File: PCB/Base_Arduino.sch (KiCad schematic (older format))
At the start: 16 parts, among them IC1 ATMEGA328-P, X1 CRYSTAL

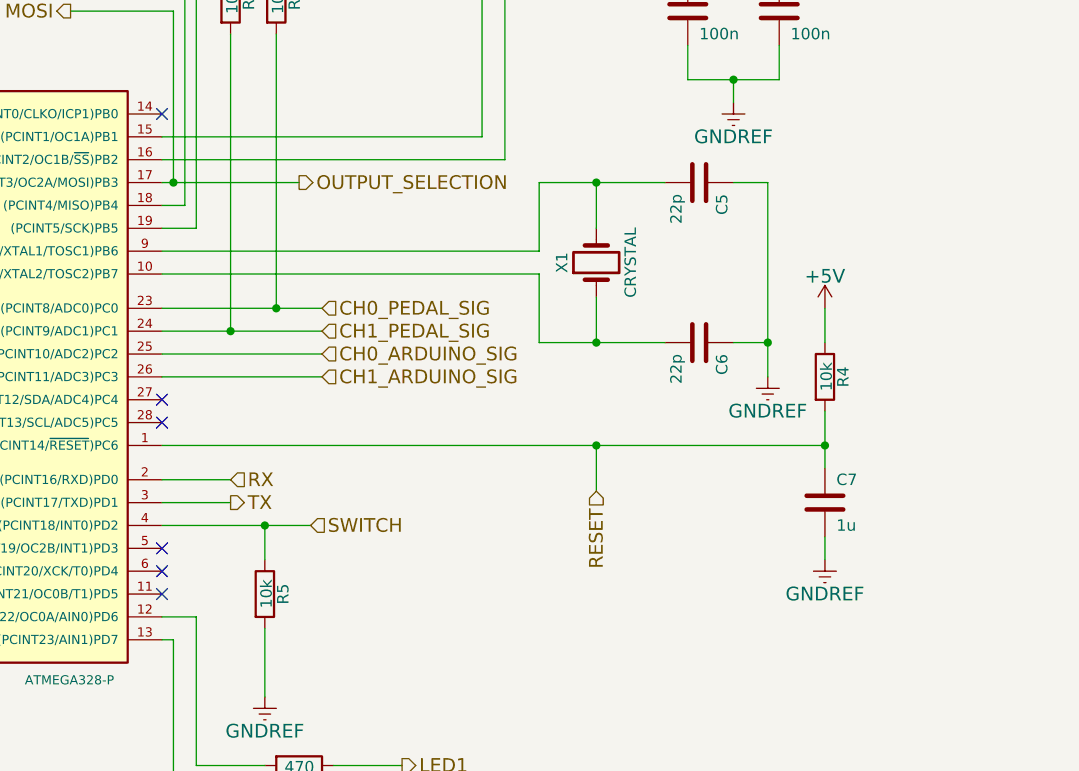
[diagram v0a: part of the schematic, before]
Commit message: Optional crystal resistor.
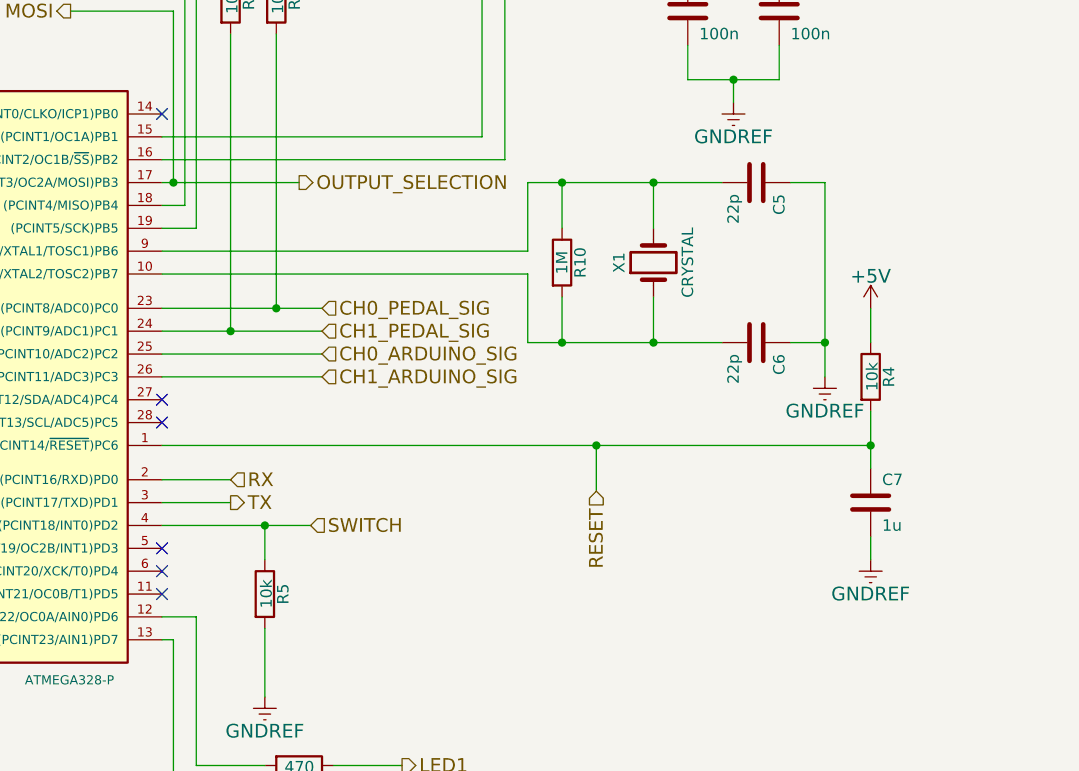
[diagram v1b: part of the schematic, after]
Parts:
- added R10: 1M, symbol R
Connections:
- net at C6.2, IC1.10 ((PCINT7/XTAL2/TOSC2)PB7), X1.1: now also R10.2
- net at C5.2, IC1.9 ((PCINT6/XTAL1/TOSC1)PB6), X1.2: now also R10.1
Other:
- moved on the sheet: C5, C6, C7, R4, X1
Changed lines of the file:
@@
 $EndComp
 $Comp
-L GNDREF #PWR015
+L GNDREF #PWR15
 U 1 1 54D7F6B2
 P 2550 5150
-F 0 "#PWR015" H 2550 4900 60  0001 C CNN
+F 0 "#PWR15" H 2550 4900 60  0001 C CNN
 F 1 "GNDREF" H 2550 5000 60  0000 C CNN
 F 2 "" H 2550 5150 60  0000 C CNN
@@
 NoConn ~ 2700 3250
 $Comp
-L +5V #PWR016
+L +5V #PWR14
 U 1 1 54D7F7B3
 P 2550 2300
-F 0 "#PWR016" H 2550 2150 60  0001 C CNN
+F 0 "#PWR14" H 2550 2150 60  0001 C CNN
 F 1 "+5V" H 2550 2440 60  0000 C CNN
 F 2 "" H 2550 2300 60  0000 C CNN
@@
 L Crystal X1
 U 1 1 54D7F8BC
-P 6500 3300
-F 0 "X1" H 6500 3450 50  0000 C CNN
-F 1 "CRYSTAL" H 6500 3150 50  0000 C CNN
-F 2 "Crystals:Crystal_HC50-U_Vertical" H 6500 3300 60  0001 C CNN
-F 3 "" H 6500 3300 60  0000 C CNN
-	1    6500 3300
+P 6750 3300
+F 0 "X1" H 6750 3450 50  0000 C CNN
+F 1 "CRYSTAL" H 6750 3150 50  0000 C CNN
+F 2 "Crystals:Crystal_HC50-U_Vertical" H 6750 3300 60  0001 C CNN
+F 3 "" H 6750 3300 60  0000 C CNN
+	1    6750 3300
 	0    -1   -1   0
 $EndComp
@@
 L C C5
 U 1 1 54D7FA47
-P 6950 2950
-F 0 "C5" H 7000 3050 50  0000 L CNN
-F 1 "22p" H 7000 2850 50  0000 L CNN
-F 2 "Capacitors_ThroughHole:C_Rect_L7_W2_P5" H 6988 2800 30  0001 C CNN
-F 3 "" H 6950 2950 60  0000 C CNN
-	1    6950 2950
+P 7200 2950
+F 0 "C5" H 7250 3050 50  0000 L CNN
+F 1 "22p" H 7250 2850 50  0000 L CNN
+F 2 "Capacitors_ThroughHole:C_Rect_L7_W2_P5" H 7238 2800 30  0001 C CNN
+F 3 "" H 7200 2950 60  0000 C CNN
+	1    7200 2950
 	0    1    1    0
 $EndComp
@@
 L C C6
 U 1 1 54D7FAD7
-P 6950 3650
-F 0 "C6" H 7000 3750 50  0000 L CNN
-F 1 "22p" H 7000 3550 50  0000 L CNN
-F 2 "Capacitors_ThroughHole:C_Rect_L7_W2_P5" H 6988 3500 30  0001 C CNN
-F 3 "" H 6950 3650 60  0000 C CNN
-	1    6950 3650
-	0    1    1    0
-$EndComp
-$Comp
-L GNDREF #PWR017
+P 7200 3650
+F 0 "C6" H 7250 3750 50  0000 L CNN
+F 1 "22p" H 7250 3550 50  0000 L CNN
+F 2 "Capacitors_ThroughHole:C_Rect_L7_W2_P5" H 7238 3500 30  0001 C CNN
+F 3 "" H 7200 3650 60  0000 C CNN
+	1    7200 3650
+	0    1    1    0
+$EndComp
+$Comp
+L GNDREF #PWR19
 U 1 1 54D7FB6B
-P 7250 3800
-F 0 "#PWR017" H 7250 3550 60  0001 C CNN
-F 1 "GNDREF" H 7250 3650 60  0000 C CNN
-F 2 "" H 7250 3800 60  0000 C CNN
-F 3 "" H 7250 3800 60  0000 C CNN
-	1    7250 3800
-	1    0    0    -1
-$EndComp
-$Comp
-L GNDREF #PWR018
+P 7500 3800
+F 0 "#PWR19" H 7500 3550 60  0001 C CNN
+F 1 "GNDREF" H 7500 3650 60  0000 C CNN
+F 2 "" H 7500 3800 60  0000 C CNN
+F 3 "" H 7500 3800 60  0000 C CNN
+	1    7500 3800
+	1    0    0    -1
+$EndComp
+$Comp
+L GNDREF #PWR21
 U 1 1 54D7FCBC
-P 7500 4600
-F 0 "#PWR018" H 7500 4350 60  0001 C CNN
-F 1 "GNDREF" H 7500 4450 60  0000 C CNN
-F 2 "" H 7500 4600 60  0000 C CNN
-F 3 "" H 7500 4600 60  0000 C CNN
-	1    7500 4600
-	1    0    0    -1
-$EndComp
-$Comp
-L +5V #PWR019
+P 7700 4600
+F 0 "#PWR21" H 7700 4350 60  0001 C CNN
+F 1 "GNDREF" H 7700 4450 60  0000 C CNN
+F 2 "" H 7700 4600 60  0000 C CNN
+F 3 "" H 7700 4600 60  0000 C CNN
+	1    7700 4600
+	1    0    0    -1
+$EndComp
+$Comp
+L +5V #PWR20
 U 1 1 54D7FCD0
-P 7500 3500
-F 0 "#PWR019" H 7500 3350 60  0001 C CNN
-F 1 "+5V" H 7500 3640 60  0000 C CNN
-F 2 "" H 7500 3500 60  0000 C CNN
-F 3 "" H 7500 3500 60  0000 C CNN
-	1    7500 3500
+P 7700 3500
+F 0 "#PWR20" H 7700 3350 60  0001 C CNN
+F 1 "+5V" H 7700 3640 60  0000 C CNN
+F 2 "" H 7700 3500 60  0000 C CNN
+F 3 "" H 7700 3500 60  0000 C CNN
+	1    7700 3500
 	1    0    0    -1
 $EndComp
@@
 L C C7
 U 1 1 54D7FCE4
-P 7500 4350
-F 0 "C7" H 7550 4450 50  0000 L CNN
-F 1 "1u" H 7550 4250 50  0000 L CNN
-F 2 "Capacitors_ThroughHole:C_Rect_L7_W4.5_P5" H 7538 4200 30  0001 C CNN
-F 3 "" H 7500 4350 60  0000 C CNN
-	1    7500 4350
+P 7700 4350
+F 0 "C7" H 7750 4450 50  0000 L CNN
+F 1 "1u" H 7750 4250 50  0000 L CNN
+F 2 "Capacitors_ThroughHole:C_Rect_L7_W4.5_P5" H 7738 4200 30  0001 C CNN
+F 3 "" H 7700 4350 60  0000 C CNN
+	1    7700 4350
 	1    0    0    -1
 $EndComp
@@
 L R R4
 U 1 1 54D7FD1C
-P 7500 3800
-F 0 "R4" V 7580 3800 50  0000 C CNN
-F 1 "10k" V 7507 3801 50  0000 C CNN
-F 2 "Discret:R3" V 7430 3800 30  0001 C CNN
-F 3 "" H 7500 3800 30  0000 C CNN
-	1    7500 3800
+P 7700 3800
+F 0 "R4" V 7780 3800 50  0000 C CNN
+F 1 "10k" V 7707 3801 50  0000 C CNN
+F 2 "Discret:R3" V 7630 3800 30  0001 C CNN
+F 3 "" H 7700 3800 30  0000 C CNN
+	1    7700 3800
 	1    0    0    -1
 $EndComp
@@
 $EndComp
 $Comp
-L GNDREF #PWR020
+L GNDREF #PWR17
 U 1 1 54D8038E
 P 5050 5200
-F 0 "#PWR020" H 5050 4950 60  0001 C CNN
+F 0 "#PWR17" H 5050 4950 60  0001 C CNN
 F 1 "GNDREF" H 5050 5050 60  0000 C CNN
 F 2 "" H 5050 5200 60  0000 C CNN
@@
 $EndComp
 $Comp
-L +5V #PWR021
+L +5V #PWR16
 U 1 1 54D80C81
 P 5000 1700
-F 0 "#PWR021" H 5000 1550 60  0001 C CNN
+F 0 "#PWR16" H 5000 1550 60  0001 C CNN
 F 1 "+5V" H 5000 1840 60  0000 C CNN
 F 2 "" H 5000 1700 60  0000 C CNN
@@
 $EndComp
 $Comp
-L GNDREF #PWR022
+L GNDREF #PWR18
 U 1 1 54D8194E
 P 7100 2600
-F 0 "#PWR022" H 7100 2350 60  0001 C CNN
+F 0 "#PWR18" H 7100 2350 60  0001 C CNN
 F 1 "GNDREF" H 7100 2450 60  0000 C CNN
 F 2 "" H 7100 2600 60  0000 C CNN
@@
 CH0_ARDUINO_SIG
 $Comp
-L +5V #PWR023
+L +5V #PWR12
 U 1 1 57BC9586
 P 1650 3400
-F 0 "#PWR023" H 1650 3250 60  0001 C CNN
+F 0 "#PWR12" H 1650 3250 60  0001 C CNN
 F 1 "+5V" H 1650 3540 60  0000 C CNN
 F 2 "" H 1650 3400 60  0000 C CNN
@@
 $EndComp
 $Comp
-L GNDREF #PWR024
+L GNDREF #PWR13
 U 1 1 57BC95BE
 P 1650 3800
-F 0 "#PWR024" H 1650 3550 60  0001 C CNN
+F 0 "#PWR13" H 1650 3550 60  0001 C CNN
 F 1 "GNDREF" H 1650 3650 60  0000 C CNN
 F 2 "" H 1650 3800 60  0000 C CNN
@@
 Connection ~ 2550 2650
 Wire Wire Line
-	4600 3350 6250 3350
-Wire Wire Line
-	6250 3350 6250 3650
-Wire Wire Line
-	6250 3650 6800 3650
-Wire Wire Line
-	6500 3450 6500 3650
-Wire Wire Line
-	4600 3250 6250 3250
-Wire Wire Line
-	6250 3250 6250 2950
-Wire Wire Line
-	6250 2950 6800 2950
-Wire Wire Line
-	6500 2950 6500 3150
-Connection ~ 6500 3650
-Connection ~ 6500 2950
-Wire Wire Line
-	7250 2950 7250 3800
-Wire Wire Line
-	7100 2950 7250 2950
-Wire Wire Line
-	7100 3650 7250 3650
-Connection ~ 7250 3650
-Wire Wire Line
-	7500 4500 7500 4600
-Wire Wire Line
-	7500 3950 7500 4200
-Wire Wire Line
-	7500 3500 7500 3650
-Wire Wire Line
-	4600 4100 7500 4100
-Connection ~ 7500 4100
+	6200 3650 7050 3650
+Wire Wire Line
+	6750 3450 6750 3650
+Wire Wire Line
+	6200 2950 7050 2950
+Wire Wire Line
+	6750 2950 6750 3150
+Connection ~ 6750 3650
+Connection ~ 6750 2950
+Wire Wire Line
+	7500 2950 7500 3800
+Wire Wire Line
+	7350 2950 7500 2950
+Wire Wire Line
+	7350 3650 7500 3650
+Connection ~ 7500 3650
+Wire Wire Line
+	7700 4500 7700 4600
+Wire Wire Line
+	7700 3950 7700 4200
+Wire Wire Line
+	7700 3500 7700 3650
+Wire Wire Line
+	4600 4100 7700 4100
+Connection ~ 7700 4100
 Wire Wire Line
 	4600 4950 4650 4950
@@
 Wire Wire Line
 	4600 3800 5300 3800
+Wire Wire Line
+	6200 2950 6200 3250
+Wire Wire Line
+	6200 3650 6200 3350
+Wire Wire Line
+	6200 3350 4600 3350
+Wire Wire Line
+	6200 3250 4600 3250
+$Comp
+L R R10
+U 1 1 57BF3972
+P 6350 3300
+F 0 "R10" V 6430 3300 50  0000 C CNN
+F 1 "1M" V 6350 3300 50  0000 C CNN
+F 2 "" V 6280 3300 50  0000 C CNN
+F 3 "" H 6350 3300 50  0000 C CNN
+	1    6350 3300
+	1    0    0    -1
+$EndComp
+Wire Wire Line
+	6350 3150 6350 2950
+Connection ~ 6350 2950
+Wire Wire Line
+	6350 3450 6350 3650
+Connection ~ 6350 3650
 $EndSCHEMATC

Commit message: Resistor footprint.
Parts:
- R10: footprint (none) -> Discret:R3
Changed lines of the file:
@@
 $EndComp
 $Comp
-L GNDREF #PWR15
+L GNDREF #PWR015
 U 1 1 54D7F6B2
 P 2550 5150
-F 0 "#PWR15" H 2550 4900 60  0001 C CNN
+F 0 "#PWR015" H 2550 4900 60  0001 C CNN
 F 1 "GNDREF" H 2550 5000 60  0000 C CNN
 F 2 "" H 2550 5150 60  0000 C CNN
@@
 NoConn ~ 2700 3250
 $Comp
-L +5V #PWR14
+L +5V #PWR016
 U 1 1 54D7F7B3
 P 2550 2300
-F 0 "#PWR14" H 2550 2150 60  0001 C CNN
+F 0 "#PWR016" H 2550 2150 60  0001 C CNN
 F 1 "+5V" H 2550 2440 60  0000 C CNN
 F 2 "" H 2550 2300 60  0000 C CNN
@@
 $EndComp
 $Comp
-L GNDREF #PWR19
+L GNDREF #PWR017
 U 1 1 54D7FB6B
 P 7500 3800
-F 0 "#PWR19" H 7500 3550 60  0001 C CNN
+F 0 "#PWR017" H 7500 3550 60  0001 C CNN
 F 1 "GNDREF" H 7500 3650 60  0000 C CNN
 F 2 "" H 7500 3800 60  0000 C CNN
@@
 $EndComp
 $Comp
-L GNDREF #PWR21
+L GNDREF #PWR018
 U 1 1 54D7FCBC
 P 7700 4600
-F 0 "#PWR21" H 7700 4350 60  0001 C CNN
+F 0 "#PWR018" H 7700 4350 60  0001 C CNN
 F 1 "GNDREF" H 7700 4450 60  0000 C CNN
 F 2 "" H 7700 4600 60  0000 C CNN
@@
 $EndComp
 $Comp
-L +5V #PWR20
+L +5V #PWR019
 U 1 1 54D7FCD0
 P 7700 3500
-F 0 "#PWR20" H 7700 3350 60  0001 C CNN
+F 0 "#PWR019" H 7700 3350 60  0001 C CNN
 F 1 "+5V" H 7700 3640 60  0000 C CNN
 F 2 "" H 7700 3500 60  0000 C CNN
@@
 $EndComp
 $Comp
-L GNDREF #PWR17
+L GNDREF #PWR020
 U 1 1 54D8038E
 P 5050 5200
-F 0 "#PWR17" H 5050 4950 60  0001 C CNN
+F 0 "#PWR020" H 5050 4950 60  0001 C CNN
 F 1 "GNDREF" H 5050 5050 60  0000 C CNN
 F 2 "" H 5050 5200 60  0000 C CNN
@@
 $EndComp
 $Comp
-L +5V #PWR16
+L +5V #PWR021
 U 1 1 54D80C81
 P 5000 1700
-F 0 "#PWR16" H 5000 1550 60  0001 C CNN
+F 0 "#PWR021" H 5000 1550 60  0001 C CNN
 F 1 "+5V" H 5000 1840 60  0000 C CNN
 F 2 "" H 5000 1700 60  0000 C CNN
@@
 $EndComp
 $Comp
-L GNDREF #PWR18
+L GNDREF #PWR022
 U 1 1 54D8194E
 P 7100 2600
-F 0 "#PWR18" H 7100 2350 60  0001 C CNN
+F 0 "#PWR022" H 7100 2350 60  0001 C CNN
 F 1 "GNDREF" H 7100 2450 60  0000 C CNN
 F 2 "" H 7100 2600 60  0000 C CNN
@@
 CH0_ARDUINO_SIG
 $Comp
-L +5V #PWR12
+L +5V #PWR023
 U 1 1 57BC9586
 P 1650 3400
-F 0 "#PWR12" H 1650 3250 60  0001 C CNN
+F 0 "#PWR023" H 1650 3250 60  0001 C CNN
 F 1 "+5V" H 1650 3540 60  0000 C CNN
 F 2 "" H 1650 3400 60  0000 C CNN
@@
 $EndComp
 $Comp
-L GNDREF #PWR13
+L GNDREF #PWR024
 U 1 1 57BC95BE
 P 1650 3800
-F 0 "#PWR13" H 1650 3550 60  0001 C CNN
+F 0 "#PWR024" H 1650 3550 60  0001 C CNN
 F 1 "GNDREF" H 1650 3650 60  0000 C CNN
 F 2 "" H 1650 3800 60  0000 C CNN
@@
 F 0 "R10" V 6430 3300 50  0000 C CNN
 F 1 "1M" V 6350 3300 50  0000 C CNN
-F 2 "" V 6280 3300 50  0000 C CNN
+F 2 "Discret:R3" V 6280 3300 50  0001 C CNN
 F 3 "" H 6350 3300 50  0000 C CNN
 	1    6350 3300

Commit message: New crystal footprint. New route.
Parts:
- X1: footprint Crystals:Crystal_HC50-U_Vertical -> Crystals:HC-49V
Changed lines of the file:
@@
 F 0 "X1" H 6750 3450 50  0000 C CNN
 F 1 "CRYSTAL" H 6750 3150 50  0000 C CNN
-F 2 "Crystals:Crystal_HC50-U_Vertical" H 6750 3300 60  0001 C CNN
+F 2 "Crystals:HC-49V" H 6750 3300 60  0001 C CNN
 F 3 "" H 6750 3300 60  0000 C CNN
 	1    6750 3300

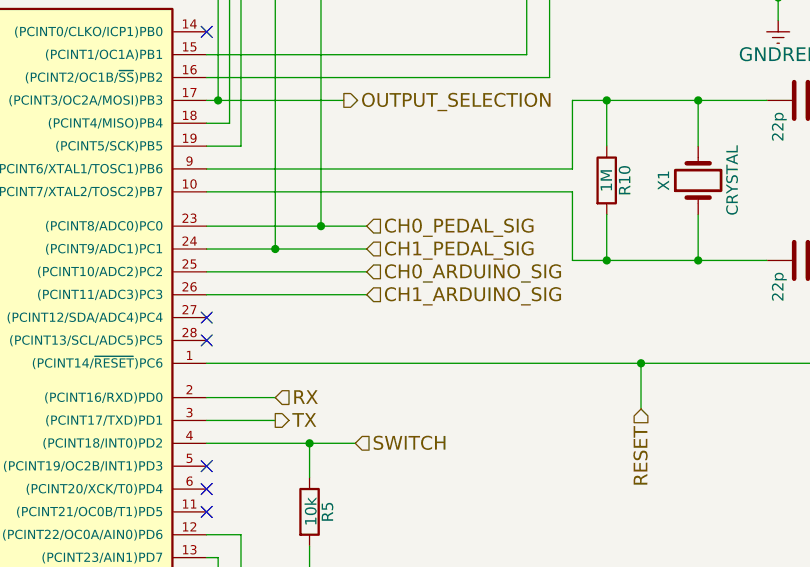
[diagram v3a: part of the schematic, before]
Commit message: Initial output feedback connection  correction.
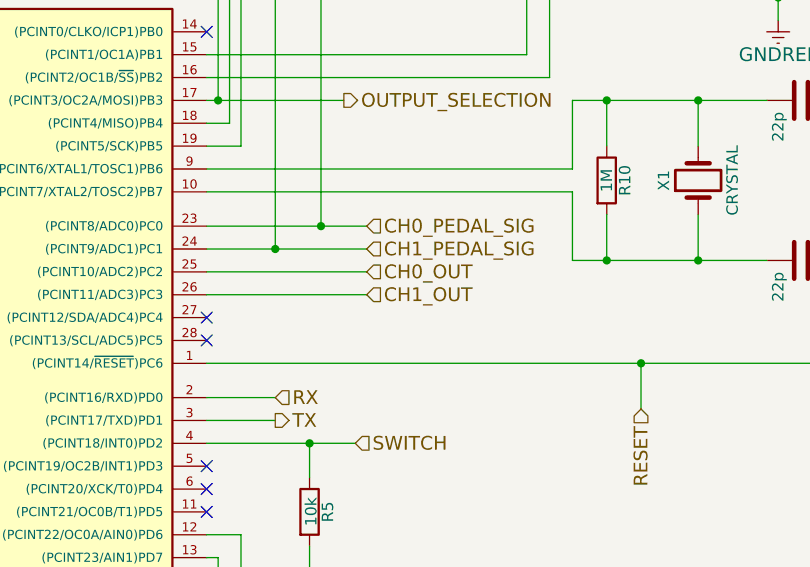
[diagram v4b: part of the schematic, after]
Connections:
- net CH0_ARDUINO_SIG: no longer IC1.25 ((PCINT10/ADC2)PC2)
- net CH1_ARDUINO_SIG: no longer IC1.26 ((PCINT11/ADC3)PC3)
- new net CH0_OUT: IC1.25 ((PCINT10/ADC2)PC2)
- new net CH1_OUT: IC1.26 ((PCINT11/ADC3)PC3)
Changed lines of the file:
@@
 Connection ~ 4900 3600
 Text HLabel 5300 3700 2    60   Input ~ 0
-CH0_ARDUINO_SIG
+CH0_OUT
 Text HLabel 5300 3800 2    60   Input ~ 0
-CH1_ARDUINO_SIG
-Wire Wire Line
-	5300 3700 4600 3700
-Wire Wire Line
-	4600 3800 5300 3800
+CH1_OUT
 Wire Wire Line
 	6200 2950 6200 3250
@@
 	6350 3450 6350 3650
 Connection ~ 6350 3650
+Wire Wire Line
+	4600 3700 5300 3700
+Wire Wire Line
+	5300 3800 4600 3800
 $EndSCHEMATC

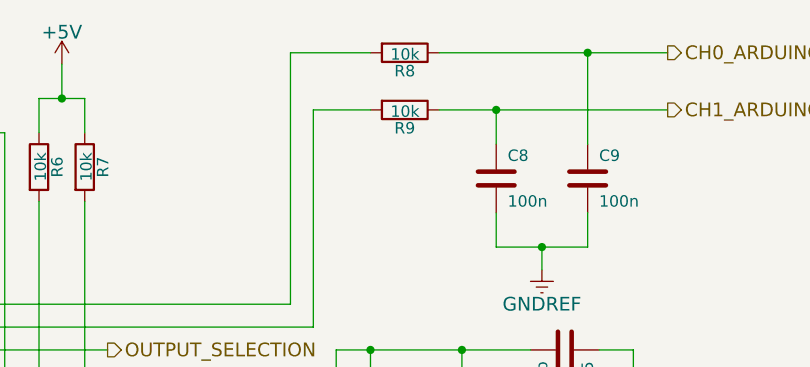
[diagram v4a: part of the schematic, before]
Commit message: Changed DAC resistor to 100k (to works fine with new 10-bit PWM and new frenquency[15khz])
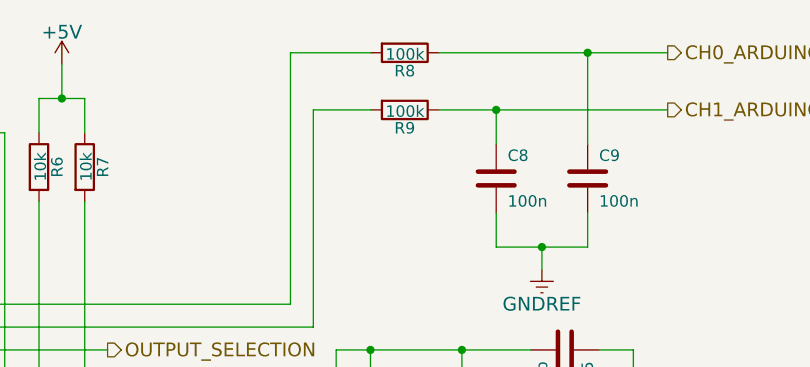
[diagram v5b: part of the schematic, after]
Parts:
- R8, R9: value 10k -> 100k
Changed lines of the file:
@@
 P 6500 1650
 F 0 "R8" V 6580 1650 50  0000 C CNN
-F 1 "10k" V 6507 1651 50  0000 C CNN
+F 1 "100k" V 6507 1651 50  0000 C CNN
 F 2 "Discret:R3" V 6430 1650 30  0001 C CNN
 F 3 "" H 6500 1650 30  0000 C CNN
@@
 P 6500 1900
 F 0 "R9" V 6580 1900 50  0000 C CNN
-F 1 "10k" V 6507 1901 50  0000 C CNN
+F 1 "100k" V 6507 1901 50  0000 C CNN
 F 2 "Discret:R3" V 6430 1900 30  0001 C CNN
 F 3 "" H 6500 1900 30  0000 C CNN

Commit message: Last commit before Mux/Demux removel. Single layer PCB incompete (3 wires). Add ADC input filter.
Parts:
- added C6: 100n, Capacitors_THT:C_Rect_L7.0mm_W2.5mm_P5.00mm, symbol C
- added C8, C9: 1n, Capacitors_THT:C_Rect_L7.0mm_W2.0mm_P5.00mm, symbol C
- added R10, R9: 2.2k, Resistors_THT:R_Axial_DIN0207_L6.3mm_D2.5mm_P7.62mm_Horizontal, symbol R
- C10: renamed from C8; footprint Capacitors_ThroughHole:C_Rect_L7_W2.5_P5 -> Capacitors_THT:C_Rect_L7.0mm_W2.5mm_P5.00mm
- C11: renamed from C9; footprint Capacitors_ThroughHole:C_Rect_L7_W2.5_P5 -> Capacitors_THT:C_Rect_L7.0mm_W2.5mm_P5.00mm
- C12: renamed from C5; footprint Capacitors_ThroughHole:C_Rect_L7_W2_P5 -> Capacitors_THT:C_Rect_L7.0mm_W2.0mm_P5.00mm
- C13: renamed from C6; footprint Capacitors_ThroughHole:C_Rect_L7_W2_P5 -> Capacitors_THT:C_Rect_L7.0mm_W2.0mm_P5.00mm
- C5: renamed from C10; footprint Capacitors_ThroughHole:C_Rect_L7_W2.5_P5 -> Capacitors_THT:C_Rect_L7.0mm_W2.5mm_P5.00mm
- C7: value 1u -> 100n; footprint Capacitors_ThroughHole:C_Rect_L7_W4.5_P5 -> Capacitors_THT:C_Rect_L7.0mm_W2.5mm_P5.00mm
- R11: renamed from R4; footprint Discret:R3 -> Resistors_THT:R_Axial_DIN0207_L6.3mm_D2.5mm_P2.54mm_Vertical
- R12: renamed from R10; footprint Discret:R3 -> Resistors_THT:R_Axial_DIN0207_L6.3mm_D2.5mm_P2.54mm_Vertical
- R2: renamed from R6; footprint Discret:R3 -> Resistors_THT:R_Axial_DIN0207_L6.3mm_D2.5mm_P2.54mm_Vertical
- R3: renamed from R7; footprint Discret:R3 -> Resistors_THT:R_Axial_DIN0207_L6.3mm_D2.5mm_P2.54mm_Vertical
- R4: renamed from R5; footprint Discret:R3 -> Resistors_THT:R_Axial_DIN0207_L6.3mm_D2.5mm_P2.54mm_Vertical
- R5: renamed from R2; footprint Discret:R3 -> Resistors_THT:R_Axial_DIN0207_L6.3mm_D2.5mm_P2.54mm_Vertical
- R6: renamed from R3; footprint Discret:R3 -> Resistors_THT:R_Axial_DIN0207_L6.3mm_D2.5mm_P2.54mm_Vertical
- R7: renamed from R8; footprint Discret:R3 -> Resistors_THT:R_Axial_DIN0207_L6.3mm_D2.5mm_P2.54mm_Vertical
- R8: renamed from R9; footprint Discret:R3 -> Resistors_THT:R_Axial_DIN0207_L6.3mm_D2.5mm_P2.54mm_Vertical
- X1: footprint Crystals:HC-49V -> Crystals:Crystal_HC49-U_Vertical
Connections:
- net CH0_PEDAL_SIG: now also C8.1, R9.1; no longer IC1.23 ((PCINT8/ADC0)PC0), R3.2
- net CH1_PEDAL_SIG: now also C9.1, R10.1; no longer IC1.24 ((PCINT9/ADC1)PC1), R2.2
- net GNDREF: now also C6.2, C8.2, C9.2
- net RESET: no longer C7.1
- new net: C6.1, IC1.23 ((PCINT8/ADC0)PC0), R3.2, R9.2
- new net: C7.1, IC1.24 ((PCINT9/ADC1)PC1), R10.2, R2.2
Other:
- moved on the sheet: C10, C11, C12, C13, R11, R12, R4, X1
